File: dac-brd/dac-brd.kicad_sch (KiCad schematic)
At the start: 18 parts, among them J1 HTR, J3 UART, U1 REF5030ID, U2 DAC5578xPW, U3 DAC5578xPW

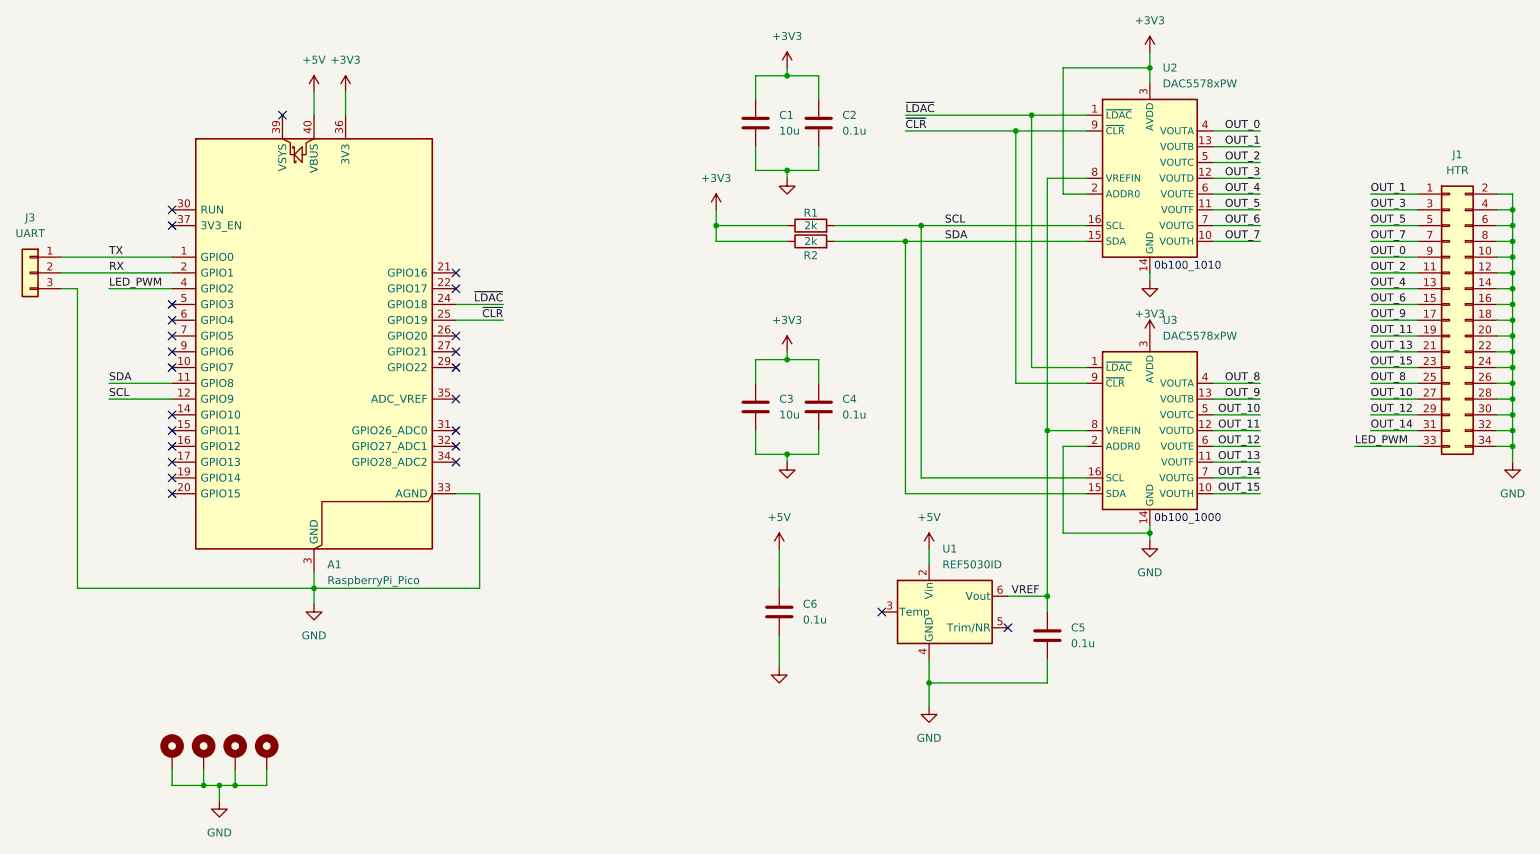
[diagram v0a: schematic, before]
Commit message: Finished mezzanine layout
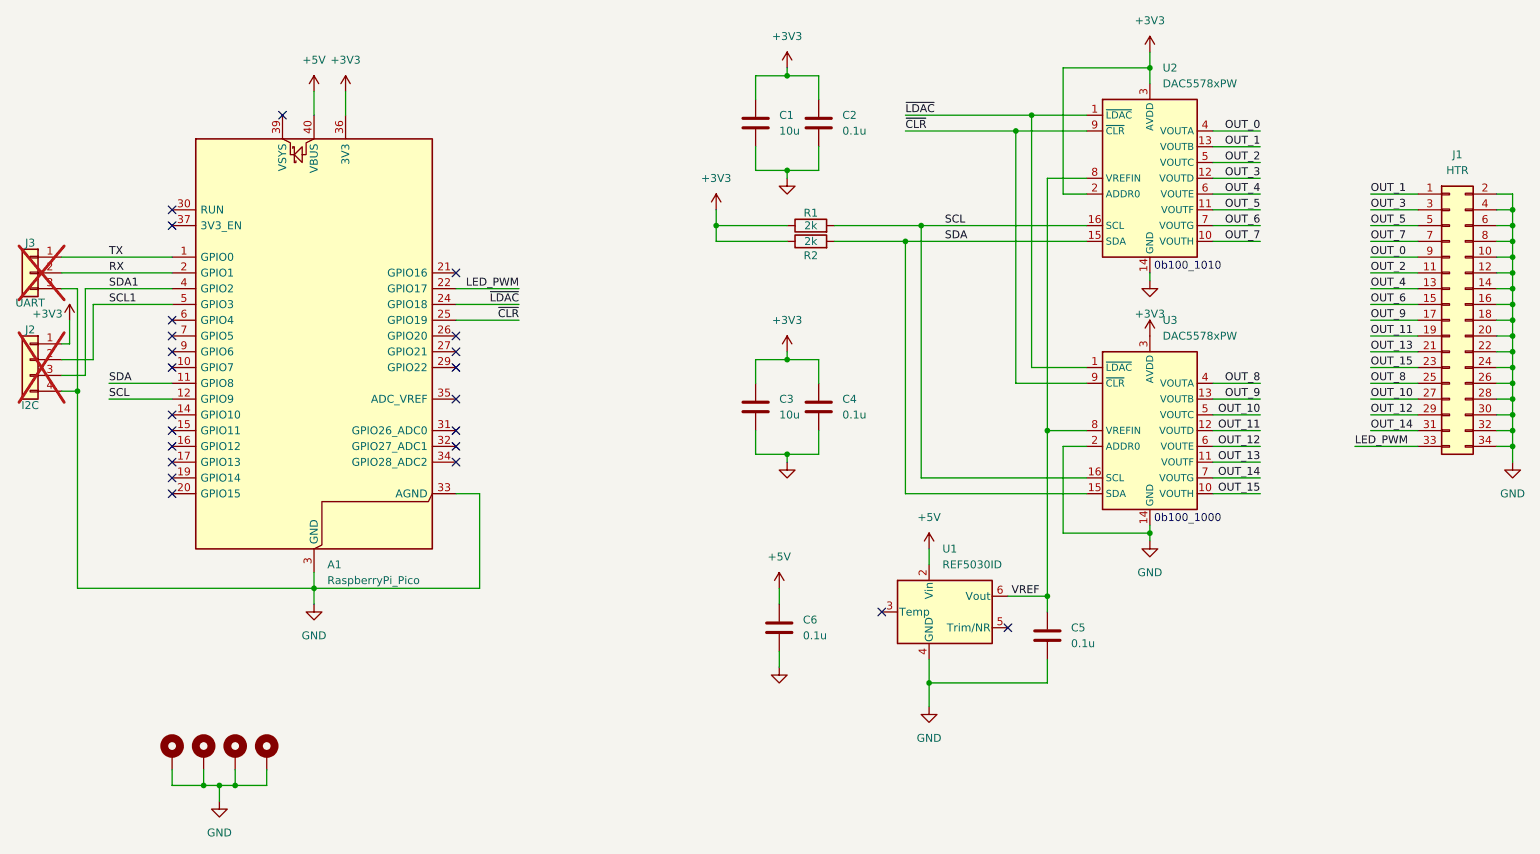
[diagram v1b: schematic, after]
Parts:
- added J2: I2C, Connector_PinHeader_2.54mm:PinHeader_1x04_P2.54mm_Vertical, symbol Connector_Generic:Conn_01x04
- J3: now not fitted; now left out of the parts list
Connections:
- net +3V3: now also J2.1 (Pin_1)
- net GND: now also J2.4 (Pin_4)
- net LED_PWM: now also A1.22 (GPIO17); no longer A1.4 (GPIO2)
- net SCL1: now reaches A1.5 (GPIO3)
- net SCL1: now also J2.2 (Pin_2)
- new net SDA1: A1.4 (GPIO2), J2.3 (Pin_3)
- no-connect marks 25 -> 23
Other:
- moved on the sheet: C6
